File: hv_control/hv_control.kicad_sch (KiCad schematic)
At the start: 158 parts, among them J1 DB9, J10 x, J11 Conn_02x03_Odd_Even, J12 x, J13 Conn_01x02_Male, J14 Conn_01x02_Male, J15 Conn_01x02_Male, J16 Conn_01x02_Male, J17 Conn_01x02_Male, J2 DB15, J3 INPUTS, J4 I/O, J5 USB_B_Mini, J6 Conn_01x01_Male, J7 Conn_01x01_Male, J8 Conn_02x04_Odd_Even, J9 x, K1 RELAY_DPDT, K2 RELAY_DPDT, P2 SWD, P8 CONN_01X01, Q2 BSS138, Q3 BSS138, U1 XMC4400-F100, U10 XMC1301T016F0032ABXUMA1, U11 LT1764EQ, U12 LMV331, U13 DRV8870DDA, U14 AD8226, U15 MAX3463, U18 LT1764EQ, U19 KSZ8081, U2 ips511g, U20 ETH100_MAG, U21 MAX3463, U22 MAX3463, U23 MAX3463, U3 ips511g, U4 MAX3463, U5 AD8226, U6 R-78E5.0-0.5, U7 TS321, U8 R-78E3.3-0.5, U9 ISO7321C, Y1 12MHz, Y2 25MHz

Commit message: Using falling edge of start-bit on the XMC1300 to trigger the ADC. Routed using P0.9 and CCU40_CC3.
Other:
- note added: "FIXME, C-E optocoupler xmc1300 reset Single ended current measurement. Supply xmc1300 with 5V Add connector for GNDPWR busbar Connect U10 pin12 to U10 pin13"
- note removed: "FIXME, C-E optocoupler xmc1300 reset Single ended current measurement. Supply xmc1300 with 5V Add connector for GNDPWR busbar"
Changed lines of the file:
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@@
-    (stroke (width 0) (type solid) (color 0 0 0 0))
-  )
-  (wire (pts (xy 41.91 243.84) (xy 41.91 254))
     (stroke (width 0) (type solid) (color 0 0 0 0))
   )
@@
     (stroke (width 0) (type solid) (color 0 0 0 0))
   )
+  (wire (pts (xy 41.91 254) (xy 41.91 243.84))
+    (stroke (width 0) (type solid) (color 0 0 0 0))
+  )
   (wire (pts (xy 41.91 254) (xy 41.91 361.95))
     (stroke (width 0) (type solid) (color 0 0 0 0))
@@
     (stroke (width 0) (type solid) (color 0 0 0 0))
   )
-  (wire (pts (xy 113.03 373.38) (xy 119.38 373.38))
-    (stroke (width 0) (type solid) (color 0 0 0 0))
-  )
   (wire (pts (xy 113.03 379.73) (xy 111.76 379.73))
     (stroke (width 0) (type solid) (color 0 0 0 0))
@@
     (stroke (width 0) (type solid) (color 0 0 0 0))
   )
+  (wire (pts (xy 119.38 373.38) (xy 113.03 373.38))
+    (stroke (width 0) (type solid) (color 0 0 0 0))
+  )
   (wire (pts (xy 119.38 373.38) (xy 119.38 377.19))
     (stroke (width 0) (type solid) (color 0 0 0 0))
@@
     (stroke (width 0) (type solid) (color 0 0 0 0))
   )
-  (wire (pts (xy 222.25 25.4) (xy 231.14 25.4))
-    (stroke (width 0) (type solid) (color 0 0 0 0))
-  )
   (wire (pts (xy 222.25 46.99) (xy 222.25 36.83))
     (stroke (width 0) (type solid) (color 0 0 0 0))
@@
   )
   (wire (pts (xy 227.33 345.44) (xy 223.52 345.44))
+    (stroke (width 0) (type solid) (color 0 0 0 0))
+  )
+  (wire (pts (xy 231.14 25.4) (xy 222.25 25.4))
     (stroke (width 0) (type solid) (color 0 0 0 0))
   )
@@
     (effects (font (size 1.27 1.27)) (justify right bottom))
   )
-  (text "FIXME,\n\nC-E optocoupler\nxmc1300 reset\nSingle ended current measurement.\nSupply xmc1300 with 5V\nAdd connector for GNDPWR busbar"
+  (text "FIXME,\n\nC-E optocoupler\nxmc1300 reset\nSingle ended current measurement.\nSupply xmc1300 with 5V\nAdd connector for GNDPWR busbar\nConnect U10 pin12 to U10 pin13"
     (at 400.05 29.21 0)
     (effects (font (size 1.27 1.27)) (justify left bottom))

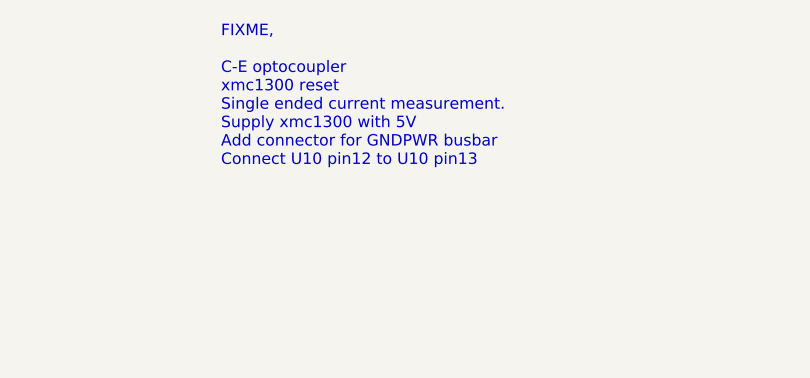
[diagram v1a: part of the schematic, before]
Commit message: MFS13 encoder using new uart driver.
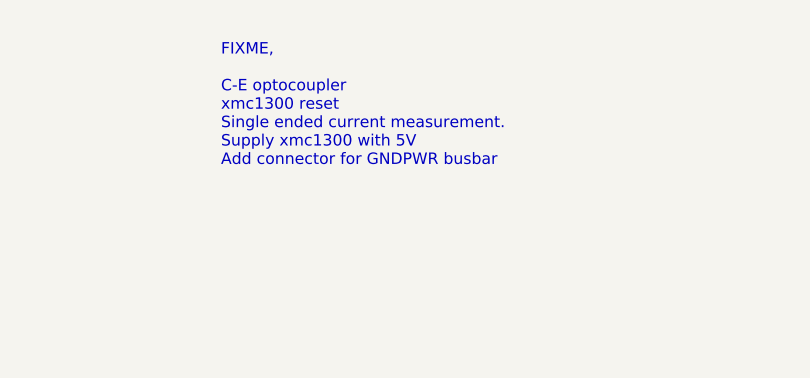
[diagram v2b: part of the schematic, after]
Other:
- note added: "FIXME, C-E optocoupler xmc1300 reset Single ended current measurement. Supply xmc1300 with 5V Add connector for GNDPWR busbar"
- note removed: "FIXME, C-E optocoupler xmc1300 reset Single ended current measurement. Supply xmc1300 with 5V Add connector for GNDPWR busbar Connect U10 pin12 to U10 pin13"
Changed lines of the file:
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@@
     (effects (font (size 1.27 1.27)) (justify right bottom))
   )
-  (text "FIXME,\n\nC-E optocoupler\nxmc1300 reset\nSingle ended current measurement.\nSupply xmc1300 with 5V\nAdd connector for GNDPWR busbar\nConnect U10 pin12 to U10 pin13"
+  (text "FIXME,\n\nC-E optocoupler\nxmc1300 reset\nSingle ended current measurement.\nSupply xmc1300 with 5V\nAdd connector for GNDPWR busbar"
     (at 400.05 29.21 0)
     (effects (font (size 1.27 1.27)) (justify left bottom))
@@
     )
     (path "/00000000-0000-0000-0000-00005e1f39b2/00000000-0000-0000-0000-00005daeb8e6"
-      (reference "R97") (unit 1) (value "150") (footprint "Resistor_SMD:R_0603_1608Metric")
+      (reference "R97") (unit 1) (value "51") (footprint "Resistor_SMD:R_0603_1608Metric")
     )
     (path "/00000000-0000-0000-0000-00005e1f39b2/00000000-0000-0000-0000-00005daeb9e9"

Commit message: Ordered new boards.
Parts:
- removed C2, C4: 100uF/35V, Capacitor_SMD:CP_Elec_8x10.5, symbol Device:CP
- removed J15: Conn_01x02_Male, Connector_PinHeader_2.54mm:PinHeader_1x02_P2.54mm_Vertical, symbol Connector:Conn_01x02_Male
- removed J6: Conn_01x01_Male, Connector_PinHeader_2.54mm:PinHeader_1x01_P2.54mm_Vertical, symbol Connector:Conn_01x01_Male
- removed P8: CONN_01X01, Connector_PinHeader_2.54mm:PinHeader_1x01_P2.54mm_Vertical, symbol Connector:Conn_01x01_Male
- removed U12: LMV331, Package_TO_SOT_SMD:SOT-23-5, symbol Comparator:LMV331
- removed VR1, VR3: PEME1-S5-S3-S, 00_Passives:RKZXXXXS, symbol Local:RKZ-1212
- added C2, C23, C4, C63: 100nF, Capacitor_SMD:C_0603_1608Metric, symbol Device:C
- added C22: C, Capacitor_THT:C_Rect_L18.0mm_W6.0mm_P15.00mm_FKS3_FKP3, symbol Device:C
- added C24: C, Capacitor_SMD:C_0603_1608Metric, symbol Device:C
- added C33: 4.7uF, Capacitor_SMD:CP_Elec_10x14.3, symbol Device:CP
- added J15, J18, J19, J6: Conn_01x01_Pin, Connector_Pin:Pin_D1.4mm_L8.5mm_W2.8mm_FlatFork, symbol Connector:Conn_01x01_Pin
- added M1: Fan_4pin, Connector:FanPinHeader_1x04_P2.54mm_Vertical, symbol Motor:Fan_4pin
- added Q1, Q4: BSS138, Package_TO_SOT_SMD:SOT-23, symbol Transistor_FET:BSS138
- added R27, R30: 27k, Resistor_SMD:R_0603_1608Metric, symbol Device:R
- added R28, R29: 3.3MEG, Resistor_SMD:R_1206_3216Metric, symbol Device:R
- added R31, R32: 120, Resistor_SMD:R_0603_1608Metric, symbol Device:R
- added R33: 62k, Resistor_SMD:R_0603_1608Metric, symbol Device:R
- added R34, R60: 1k, Resistor_SMD:R_0603_1608Metric, symbol Device:R
- added R61: 0, Resistor_SMD:R_0805_2012Metric, symbol Device:R
- added U12: TLV9064, Package_SO:SOIC-14_3.9x8.7mm_P1.27mm, symbol Amplifier_Operational:TLV9064
- HOLE3, HOLE4: footprint MountingHole:MountingHole_3.2mm_M3 -> MountingHole:MountingHole_3.2mm_M3_DIN965_Pad
- J1: symbol Local:DB9 -> 00_Home:DB9_gnd
- J13, J14, J16, J17: footprint 00_Local:pin_2_5mm -> 00_Passives:pin_2_5mm
- J2: symbol Local:DB15 -> 00_Home:DB15_gnd
- K1, K2: footprint 00_Local:T77 -> 00_Passives:T77
- R15: value R -> 3.3MEG; footprint Resistor_SMD:R_0603_1608Metric -> Resistor_SMD:R_1206_3216Metric
- R16: value R -> 27k
- U7: value TS321 -> ${SIM.PARAMS}; Spice_Node_Sequence 3,4,5,2,1 -> (none)
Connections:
- net +12V: now also M1.2 (+), R61.1
- net +24V: now also R61.2
- net +3.3VP: now also R16.2, U12.4 (V+); no longer R16.1
- net +5V: now also C2.1, C4.1, C63.1
- net +800V: now also C22.1, C33.1, J15.1 (Pin_1)
- net -12V: now also C23.2
- net GND: now also J17.1 (Pin_1), Y1.2, Y1.4, Y2.2, Y2.4, C2.2, C23.1, C4.2, M1.1 (-), Q1.2 (S), Q4.2 (S), R34.1, R60.1; no longer J16.2 (Pin_2), U15.2 (~RE), U15.3 (DE), U15.4 (DI), VR2.2 (VIN-)
- net GNDPWR: now also C22.2, C24.2, C33.2, J18.1 (Pin_1), J19.1 (Pin_1), R27.2, R30.2, U12.11 (V-)
- net I0_N: now also J10.3 (Pin_3), J12.3 (Pin_3), U12.8, U12.9 (-); no longer U10.16 (P2.6)
- net IO0: now also U1.70 (P1.13); no longer U1.78 (P1.1)
- net IO5: now also U1.83 (P1.6); no longer U1.91 (P3.5)
- net IO6: now also U1.91 (P3.5); no longer U1.92 (P3.4)
- net IO7: now also U1.92 (P3.4); no longer U1.93 (P3.3)
- net PWM0: now also U1.93 (P3.3); no longer U1.4 (P0.9)
- net at HOLE1.1: now also J1.16
- net at HOLE4.1: now also J2.16
- net at J2.14 (P14), U14.1 (-): now also R32.2
- net at J2.15 (P15), U5.1 (-): now also R31.2
- net at J2.7, U14.4 (+): now also R32.1
- net at J2.8, U5.4 (+): now also R31.1
- net ENC_REF: now reaches U14.6 (ref), U5.6 (ref), U7.1, U7.4 (-)
- net ENC_REF: now also U1.20 (P14.15)
- net COPRO_POWER: now reaches U1.3 (P0.10)
- net COPRO_POWER: now also Q4.1 (G), R60.2
- net AN_IN5: now reaches J3.1 (Pin_1), U1.26 (P14.5)
- net AN_IN4: now reaches J3.3 (Pin_3), U1.27 (P14.4)
- net AN_IN3: now reaches J3.5 (Pin_5), U1.28 (P14.3)
- net AN_IN2: now reaches J3.7 (Pin_7), U1.29 (P14.2)
- net AN_IN1: now reaches J3.9 (Pin_9), U1.30 (P14.1)
- net AN_IN0: now reaches J3.11 (Pin_11), U1.31 (P14.0)
- net ENC0_CDIR: now reaches U1.72 (P1.11)
- net ENC0_CDIR: now also U15.2 (~{RE}), U15.3 (DE)
- net fan: now reaches U1.94 (P0.12)
- net fan: now also M1.3 (Tacho)
- net at U1.96 (P0.6): now also M1.4 (PWM)
- net at U10.7 (P0.0): no longer R15.1
- net at U10.8 (P0.5): no longer R16.2
- net at R13.1, R14.1: now also C5.1, U12.5 (+)
- net at R15.2: now also J6.1 (Pin_1); no longer C5.1
- net at J16.1 (Pin_1): now also U13.8 (OUT2); no longer U13.6 (OUT1)
- removed net -3.3Vp: J10.1 (Pin_1), J12.1 (Pin_1), J9.1 (Pin_1)
- net ETH0_~RST renamed ETH0_~{RST}
- net I1_N: no longer names the net of U10.3 (P2.10)
- net I1_N: now also U12.6 (-), U12.7; no longer J10.3 (Pin_3)
- net I2_N: no longer names the net of U10.2 (P2.9)
- net I2_N: now also U12.1, U12.2 (-); no longer J12.3 (Pin_3)
- net Vfan renamed Vmeas_24
- net ~A renamed ~{A}
- net ~B renamed ~{B}
- net ~Z renamed ~{Z}
- new net: J16.2 (Pin_2), U13.6 (OUT1)
- new net: C63.2, Q4.3 (D), VR2.2 (VIN-)
- new net: C24.1, R29.1, R30.1, U12.3 (+)
- new net: R15.1, R28.2
- new net: Q1.3 (D), R33.1
- new net: R28.1, R29.2
- new net: R16.1, R27.1, U12.10 (+)
- new net ENC0_CLK: U1.78 (P1.1), U15.4 (DI)
- new net SUPPLY_VOLTAGE: Q1.1 (G), R34.2, U1.4 (P0.9)
- new net flyback/VOLTAGE: R33.2
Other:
- sheet flyback ports: added VOLTAGE; removed none
- note removed: "FIXME, C-E optocoupler xmc1300 reset Single ended current measurement. Supply xmc1300 with 5V Add connector for GNDPWR busbar"
- moved on the sheet: C36, C52, C53, C54, C55, HOLE1, HOLE3, HOLE4, J16, R22, R23

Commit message: Set the run bit in the timer for the POSIF.
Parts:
- added R62: 0, Resistor_SMD:R_0603_1608Metric, symbol Device:R
- M1: Manufacturer (none) -> Molex; Mouser (none) -> 538-47053-3000; PartNr (none) -> 47053-3000
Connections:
- net GND: now also R62.2
- net LED0: now also D1.8 (K), R5.1; no longer D1.4 (K), R2.1
- net LED1: now also D1.2 (K), R4.1; no longer D1.6 (K), R3.1
- net LED2: now also D1.6 (K), R3.1; no longer D1.2 (K), R4.1
- net LED3: now also D1.4 (K), R2.1; no longer D1.8 (K), R5.1
- net TRACED1: now also R4.2; no longer R2.2
- net TRACED3: now also R2.2; no longer R4.2
- net at HOLE4.1, J2.16: now also R62.1
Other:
- note added: "FIXME Opto pinning RXD_TIMER on P0.9 of XMC1301"
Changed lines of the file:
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@@
   (junction (at 238.76 190.5) (diameter 1.016) (color 0 0 0 0)
   )
-  (junction (at 549.91 364.49) (diameter 0) (color 0 0 0 0)
-  )
   (junction (at 387.35 299.72) (diameter 1.016) (color 0 0 0 0)
   )
@@
   (junction (at 238.76 187.96) (diameter 1.016) (color 0 0 0 0)
   )
+  (junction (at 196.85 278.13) (diameter 0) (color 0 0 0 0)
+  )
   (junction (at 208.28 193.04) (diameter 1.016) (color 0 0 0 0)
   )
@@
     (stroke (width 0) (type solid))
   )
-  (wire (pts (xy 549.91 364.49) (xy 558.8 364.49))
-    (stroke (width 0) (type default))
-  )
   (wire (pts (xy 281.94 290.83) (xy 280.67 290.83))
     (stroke (width 0) (type solid))
@@
     (stroke (width 0) (type solid))
   )
+  (wire (pts (xy 196.85 278.13) (xy 194.31 278.13))
+    (stroke (width 0) (type default))
+  )
   (wire (pts (xy 410.21 181.61) (xy 434.34 181.61))
     (stroke (width 0) (type solid))
@@
     (stroke (width 0) (type solid))
   )
-  (wire (pts (xy 549.91 364.49) (xy 549.91 365.76))
-    (stroke (width 0) (type default))
-  )
   (wire (pts (xy 306.07 184.15) (xy 323.85 184.15))
     (stroke (width 0) (type default))
@@
     (stroke (width 0) (type solid))
   )
+  (wire (pts (xy 196.85 287.02) (xy 196.85 288.29))
+    (stroke (width 0) (type default))
+  )
   (wire (pts (xy 313.69 354.33) (xy 309.88 354.33))
     (stroke (width 0) (type solid))
@@
     (stroke (width 0) (type solid))
   )
-  (wire (pts (xy 558.8 363.22) (xy 558.8 364.49))
-    (stroke (width 0) (type default))
-  )
   (wire (pts (xy 120.65 299.72) (xy 133.35 299.72))
     (stroke (width 0) (type solid))
@@
     (stroke (width 0) (type solid))
   )
-  (wire (pts (xy 389.89 260.35) (xy 400.05 260.35))
+  (wire (pts (xy 384.81 260.35) (xy 400.05 260.35))
     (stroke (width 0) (type default))
   )
@@
     (stroke (width 0) (type solid))
   )
+  (wire (pts (xy 196.85 278.13) (xy 196.85 279.4))
+    (stroke (width 0) (type default))
+  )
   (wire (pts (xy 207.01 223.52) (xy 207.01 227.33))
     (stroke (width 0) (type solid))
@@
     (stroke (width 0) (type solid))
   )
-  (wire (pts (xy 549.91 363.22) (xy 549.91 364.49))
-    (stroke (width 0) (type default))
-  )
   (wire (pts (xy 161.29 297.18) (xy 161.29 304.8))
     (stroke (width 0) (type solid))
@@
     (stroke (width 0) (type solid))
   )
-  (wire (pts (xy 199.39 278.13) (xy 194.31 278.13))
+  (wire (pts (xy 199.39 278.13) (xy 196.85 278.13))
     (stroke (width 0) (type default))
   )
@@
     (effects (font (size 1.27 1.27)) (justify left bottom))
   )
+  (text "FIXME\n\nOpto pinning\nRXD_TIMER on P0.9 of XMC1301" (at 322.58 36.83 0)
+    (effects (font (size 1.27 1.27)) (justify left bottom))
+  )
   (text "HROUT10" (at 77.47 327.66 0)
     (effects (font (size 1.27 1.27)) (justify right bottom))
@@
     (effects (font (size 1.27 1.27)) (justify left bottom))
   )
-  (label "COPRO_POWER" (at 389.89 260.35 0) (fields_autoplaced)
+  (label "COPRO_POWER" (at 384.81 260.35 0) (fields_autoplaced)
     (effects (font (size 1.27 1.27)) (justify left bottom))
   )
@@
     (effects (font (size 1.524 1.524)) (justify left bottom))
   )
-  (label "LED3" (at 152.4 325.12 0) (fields_autoplaced)
+  (label "LED3" (at 152.4 347.98 0) (fields_autoplaced)
     (effects (font (size 1.524 1.524)) (justify left bottom))
   )
@@
     (effects (font (size 1.27 1.27)) (justify left bottom))
   )
-  (label "LED1" (at 152.4 340.36 0) (fields_autoplaced)
+  (label "LED1" (at 152.4 332.74 0) (fields_autoplaced)
     (effects (font (size 1.524 1.524)) (justify left bottom))
   )
@@
     (effects (font (size 1.27 1.27)) (justify left bottom))
   )
-  (label "LED0" (at 152.4 347.98 0) (fields_autoplaced)
+  (label "LED0" (at 152.4 325.12 0) (fields_autoplaced)
     (effects (font (size 1.524 1.524)) (justify left bottom))
   )
@@
     (effects (font (size 1.524 1.524)) (justify left bottom))
   )
-  (label "TRACED3" (at 139.7 332.74 180) (fields_autoplaced)
+  (label "TRACED3" (at 139.7 347.98 180) (fields_autoplaced)
     (effects (font (size 1.27 1.27)) (justify right bottom))
   )
@@
     (effects (font (size 1.27 1.27)) (justify right bottom))
   )
-  (label "TRACED1" (at 139.7 347.98 180) (fields_autoplaced)
+  (label "TRACED1" (at 139.7 332.74 180) (fields_autoplaced)
     (effects (font (size 1.27 1.27)) (justify right bottom))
   )
@@
     (effects (font (size 1.27 1.27)) (justify left bottom))
   )
-  (label "LED2" (at 152.4 332.74 0) (fields_autoplaced)
+  (label "LED2" (at 152.4 340.36 0) (fields_autoplaced)
     (effects (font (size 1.524 1.524)) (justify left bottom))
   )
@@
       (effects (font (size 1.27 1.27)) hide)
     )
+    (property "Manufacturer" "Molex" (at 107.95 345.44 0)
+      (effects (font (size 1.27 1.27)) hide)
+    )
+    (property "Mouser" "538-47053-3000" (at 107.95 345.44 0)
+      (effects (font (size 1.27 1.27)) hide)
+    )
+    (property "PartNr" "47053-3000" (at 107.95 345.44 0)
+      (effects (font (size 1.27 1.27)) hide)
+    )
     (pin "1")
     (pin "2")
@@
     )
   )
+  (symbol (lib_id "power:GND") (at 196.85 288.29 0) (unit 1)
+    (in_bom yes) (on_board yes) (dnp no)
+    (property "Reference" "#PWR054" (at 196.85 294.64 0)
+      (effects (font (size 1.27 1.27)) hide)
+    )
+    (property "Value" "GND" (at 196.85 292.1 0)
+      (effects (font (size 1.27 1.27)))
+    )
+    (property "Footprint" "" (at 196.85 288.29 0)
+      (effects (font (size 1.27 1.27)))
+    )
+    (property "Datasheet" "" (at 196.85 288.29 0)
+      (effects (font (size 1.27 1.27)))
+    )
+    (pin "1")
+    (instances
+      (project "hv_control"
+        (path "/9cd906a6-656f-4962-bdb7-65fbbd88db52"
+          (reference "#PWR054") (unit 1)
+        )
+      )
+    )
+  )
   (symbol (lib_name "+12V_1") (lib_id "power:+12V") (at 532.13 274.32 0) (unit 1)
     (in_bom yes) (on_board yes) (dnp no)
@@
     )
   )
+  (symbol (lib_id "Device:R") (at 196.85 283.21 0) (unit 1)
+    (in_bom yes) (on_board yes) (dnp no)
+    (property "Reference" "R62" (at 198.882 283.21 90)
+      (effects (font (size 1.27 1.27)))
+    )
+    (property "Value" "0" (at 196.85 283.21 90)
+      (effects (font (size 1.27 1.27)))
+    )
+    (property "Footprint" "Resistor_SMD:R_0603_1608Metric" (at 195.072 283.21 90)
+      (effects (font (size 1.27 1.27)) hide)
+    )
+    (property "Datasheet" "~" (at 196.85 283.21 0)
+      (effects (font (size 1.27 1.27)) hide)
+    )
+    (pin "1")
+    (pin "2")
+    (instances
+      (project "hv_control"
+        (path "/9cd906a6-656f-4962-bdb7-65fbbd88db52"
+          (reference "R62") (unit 1)
+        )
+      )
+    )
+  )
   (symbol (lib_id "power:+12V") (at 107.95 337.82 0) (unit 1)
     (in_bom yes) (on_board yes) (dnp no)
@@
         )
       )
-    )
-  )
-  (symbol (lib_id "power:Earth_Protective") (at 549.91 365.76 0) (unit 1)
-    (in_bom yes) (on_board yes) (dnp no)
-    (property "Reference" "#PWR055" (at 556.26 372.11 0)
-      (effects (font (size 1.27 1.27)) hide)
-    )
-    (property "Value" "Earth_Protective" (at 561.34 369.57 0)
-      (effects (font (size 1.27 1.27)) hide)
-    )
-    (property "Footprint" "" (at 549.91 368.3 0)
-      (effects (font (size 1.27 1.27)) hide)
-    )
-    (property "Datasheet" "~" (at 549.91 368.3 0)
-      (effects (font (size 1.27 1.27)) hide)
-    )
-    (pin "1")
-    (instances
-      (project "hv_control"
-        (path "/9cd906a6-656f-4962-bdb7-65fbbd88db52"
-          (reference "#PWR055") (unit 1)
-        )
-      )

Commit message: Remarks for next version.
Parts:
- C1, C14, C19, C34, C36, C38, C6: Manufacturer (none) -> Panasonic; PartNr (none) -> EEEFK1V101P
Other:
- note added: "FIXME Opto pinning RXD_TIMER on P0.9 of XMC1301 100nF parallel with R27"
- note removed: "FIXME Opto pinning RXD_TIMER on P0.9 of XMC1301"
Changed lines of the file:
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@@
     (effects (font (size 1.27 1.27)) (justify left bottom))
   )
-  (text "FIXME\n\nOpto pinning\nRXD_TIMER on P0.9 of XMC1301" (at 322.58 36.83 0)
+  (text "FIXME\n\nOpto pinning\nRXD_TIMER on P0.9 of XMC1301\n100nF parallel with R27"
+    (at 322.58 36.83 0)
     (effects (font (size 1.27 1.27)) (justify left bottom))
   )
@@
       (effects (font (size 1.27 1.27)))
     )
+    (property "Manufacturer" "Panasonic" (at 22.86 33.02 0)
+      (effects (font (size 1.27 1.27)) hide)
+    )
+    (property "PartNr" "EEEFK1V101P" (at 22.86 33.02 0)
+      (effects (font (size 1.27 1.27)) hide)
+    )
     (pin "1")
     (pin "2")
@@
       (effects (font (size 1.27 1.27)))
     )
+    (property "Manufacturer" "Panasonic" (at 85.09 33.02 0)
+      (effects (font (size 1.27 1.27)) hide)
+    )
+    (property "PartNr" "EEEFK1V101P" (at 85.09 33.02 0)
+      (effects (font (size 1.27 1.27)) hide)
+    )
     (pin "1")
     (pin "2")
@@
       (effects (font (size 1.27 1.27)))
     )
+    (property "Manufacturer" "Panasonic" (at 181.61 33.02 0)
+      (effects (font (size 1.27 1.27)) hide)
+    )
+    (property "PartNr" "EEEFK1V101P" (at 181.61 33.02 0)
+      (effects (font (size 1.27 1.27)) hide)
+    )
     (pin "1")
     (pin "2")
@@
       (effects (font (size 1.27 1.27)))
     )
+    (property "Manufacturer" "Panasonic" (at 119.38 381 0)
+      (effects (font (size 1.27 1.27)) hide)
+    )
+    (property "PartNr" "EEEFK1V101P" (at 119.38 381 0)
+      (effects (font (size 1.27 1.27)) hide)
+    )
     (pin "1")
     (pin "2")
@@
       (effects (font (size 1.27 1.27)))
     )
+    (property "Manufacturer" "Panasonic" (at 462.28 247.65 0)
+      (effects (font (size 1.27 1.27)) hide)
+    )
+    (property "PartNr" "EEEFK1V101P" (at 462.28 247.65 0)
+      (effects (font (size 1.27 1.27)) hide)
+    )
     (pin "1")
     (pin "2")
@@
       (effects (font (size 1.27 1.27)))
     )
+    (property "Manufacturer" "Panasonic" (at 509.27 248.92 0)
+      (effects (font (size 1.27 1.27)) hide)
+    )
+    (property "PartNr" "EEEFK1V101P" (at 509.27 248.92 0)
+      (effects (font (size 1.27 1.27)) hide)
+    )
     (pin "1")
     (pin "2")
@@
       (effects (font (size 1.27 1.27)))
     )
+    (property "Manufacturer" "Panasonic" (at 510.54 304.8 0)
+      (effects (font (size 1.27 1.27)) hide)
+    )
+    (property "PartNr" "EEEFK1V101P" (at 510.54 304.8 0)
+      (effects (font (size 1.27 1.27)) hide)
+    )
     (pin "1")

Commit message: Adding initial configuration packet.
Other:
- note added: "FIXME Opto pinning RXD_TIMER on P0.9 of XMC1301 100nF parallel with R27 Gaten sub-d te klein"
- note removed: "FIXME Opto pinning RXD_TIMER on P0.9 of XMC1301 100nF parallel with R27"
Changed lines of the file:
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@@
     (effects (font (size 1.27 1.27)) (justify left bottom))
   )
-  (text "FIXME\n\nOpto pinning\nRXD_TIMER on P0.9 of XMC1301\n100nF parallel with R27"
+  (text "FIXME\n\nOpto pinning\nRXD_TIMER on P0.9 of XMC1301\n100nF parallel with R27\nGaten sub-d te klein"
     (at 322.58 36.83 0)
     (effects (font (size 1.27 1.27)) (justify left bottom))
